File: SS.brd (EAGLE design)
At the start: 100 x 100 mm, 84 parts, among them K1 4052, K2 4052, Q1 SN74AHC-OR, Q2 UMD5N, Q3 UMD5N, Q4 SN74AHC-OR, Q5 BFP460, Q7 NCP553, Q8 TBD, X1 SO-239, X2 SO-239

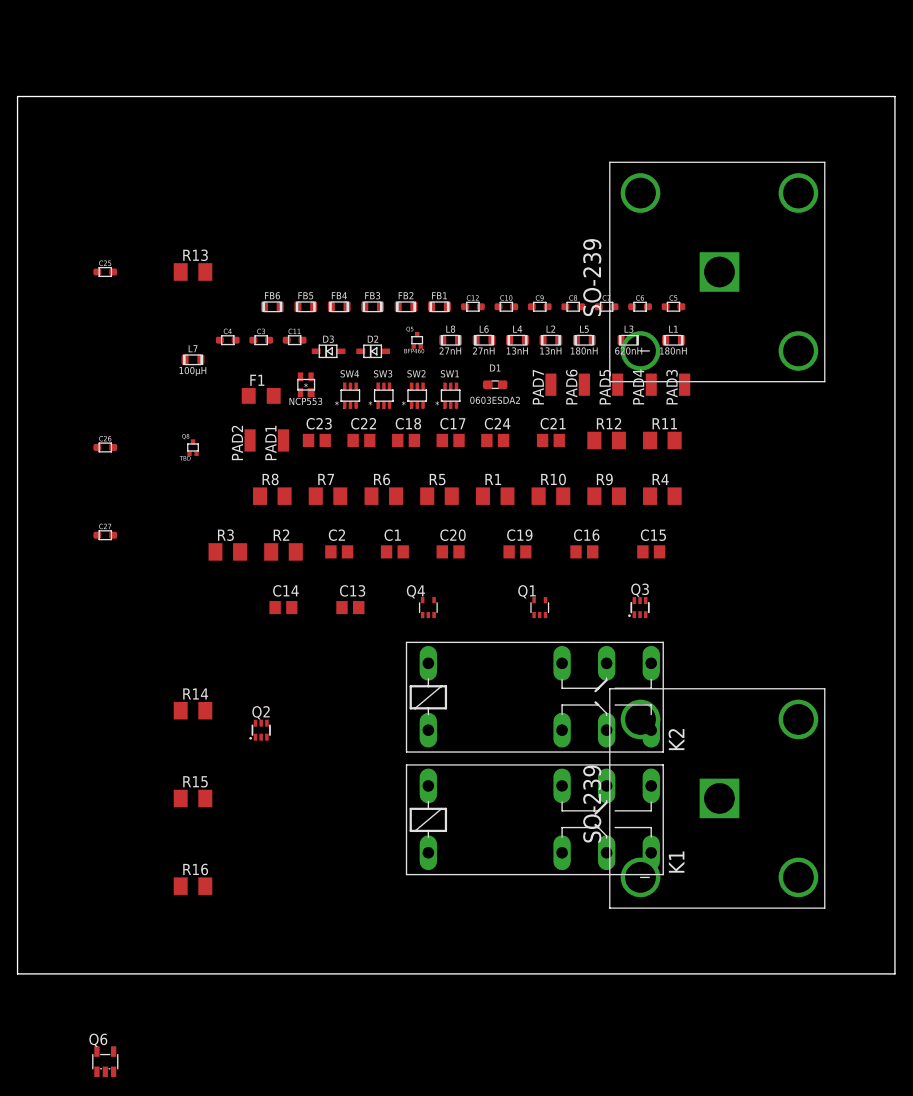
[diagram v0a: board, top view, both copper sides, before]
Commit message: Small minor improvements
* Corrected position of surge arrestor
* Added description for some networks
* Small improvements in component placement
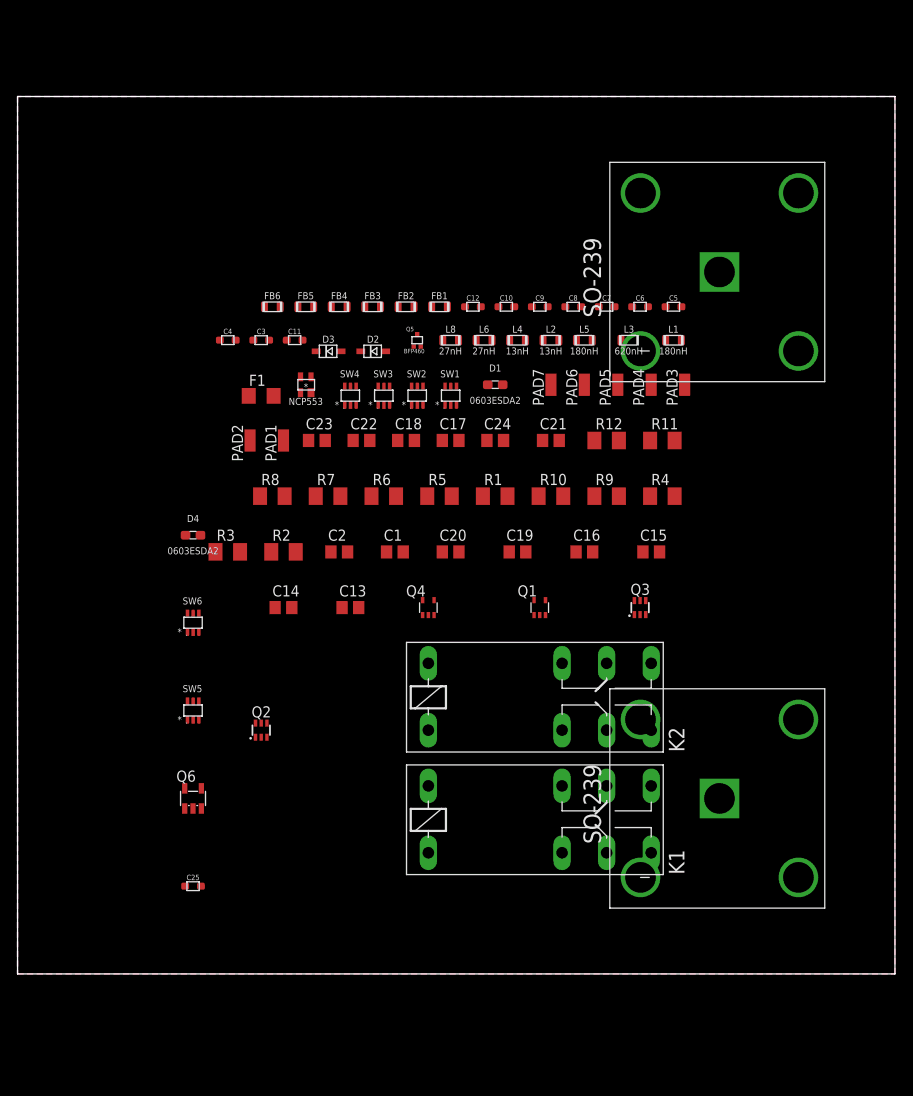
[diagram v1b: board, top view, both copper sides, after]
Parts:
- removed C26: 100pF, aarf:GRM18
- removed C27: 0.047µF, aarf:GRM18
- removed L7: 100µH, aarf:0805
- removed Q8: TBD, aarf:TSFP-3
- removed R13, R14: 4.7kΩ, rcl:M1206
- removed R15: 100Ω, rcl:M1206
- removed R16: 2.2kΩ, rcl:M1206
- added D4: 0603ESDA2, aarf:0603
- added SW5, SW6: (no value), aarf:SC-70
- C25: value 0.01µF -> 390pF
- moved C25 70.7 mm to (20.0, 10.0)
- moved Q6 31.6 mm to (20.0, 20.0)
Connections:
- net N$10 renamed LNA_IN
- net N$12 renamed FULL_BYP
- net N$15 renamed TX_INH
- net N$38 renamed BPF_OUT
- net N$43 renamed LNA_OUT
- net N$6 renamed LNA_BYPASS
- net UHF_ON renamed BPF_UHF
- removed net GPIO_OVERRIDE: FB6.P$2, Q4.2
- removed net N$29: C26.P$1, Q8.3, R16.2
- removed net N$30: C25.P$2, Q8.1, R13.2, R14.2
- removed net N$33: C27.P$2, R15.2, R16.1
- removed net N$37: C26.P$2, K1.S1, SW1.5
- removed net N$40: K2.S1, SW4.5
- new net BPF_IN: SW1.5, SW5.3
- new net FROM_BPF: D4.2, K2.S1, SW6.5
- new net LNA_OFF: Q4.4, SW3.4, SW4.4
- new net N$6: C25.P$2, SW5.5
- new net TO_BPF: C25.P$1, D1.2, K1.S1
- net 0: now also D4.1, SW5.1, SW5.2, SW6.1, SW6.2; no longer C25.P$1, C27.P$1, Q8.2, R14.1
- net 13.8V: no longer L7.P$2
- net 3V: now also SW5.6, SW6.6
- net AMP_OFF: now also FB6.P$2, Q4.2; no longer Q4.4, SW3.4, SW4.4
- net N$23: now also SW4.5, SW6.3; no longer L7.P$1, R15.1
- net N$8: no longer D1.2
- net RLY_BYPASS: now also SW5.4, SW6.4; no longer R13.1
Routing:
- added copper zone on layer 1, net GND
- added copper zone on layer 16, net GND

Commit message: More updates - refinements
* Added RF relays
* Simplified to a single relay driver (more than enough oomph to drive them both)
* New PNP-based driver for TX_GND
* Copious amount of signal direction and comments
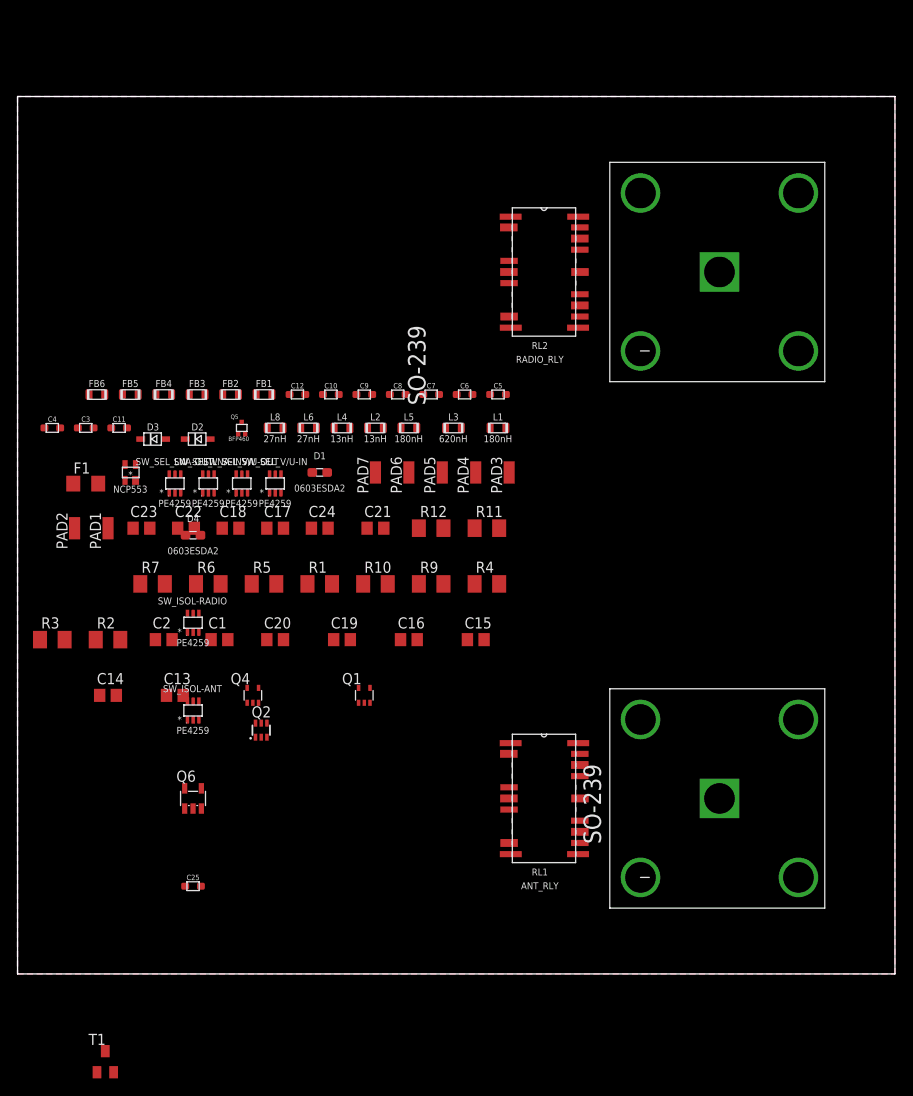
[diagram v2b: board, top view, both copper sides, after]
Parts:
- removed K1, K2: 4052, relay:F4052
- removed Q3: UMD5N, aarf:SOT363
- removed R8: 10kΩ, rcl:M1206
- removed SW1, SW2, SW3, SW4: (no value), aarf:SC-70
- added RL1: ANT_RLY, aarf:RELAY-TE-HF3
- added RL2: RADIO_RLY, aarf:RELAY-TE-HF3
- added SW_SEL_LNA-IN, SW_SEL_LNA-OUT, SW_SEL_V/U-IN, SW_SEL_V/U-OUT: PE4259, aarf:SC-70
- added T1: MMBTRA104SS, transistor:SC59-BEC
- PAD3: value RX -> TX_GND
- Q6: value (none) -> L78L05
- SW_ISOL-ANT, SW_ISOL-RADIO: value (none) -> PE4259
- moved L1 22.4 mm to (54.8, 62.2)
- moved L3 22.4 mm to (49.7, 62.2)
- moved C11 22.4 mm to (11.6, 62.2)
- moved C22 22.4 mm to (19.2, 50.8)
- moved C3 22.4 mm to (7.77, 62.2)
- moved C4 22.4 mm to (3.96, 62.2)
- moved C5 22.4 mm to (54.8, 66.0)
- moved D1 22.4 mm to (34.4, 57.1)
- moved FB1 22.4 mm to (28.1, 66.0)
- moved L2 22.4 mm to (40.8, 62.2)
- moved L4 22.4 mm to (37.0, 62.2)
- moved L6 22.4 mm to (33.2, 62.2)
- moved L8 22.4 mm to (29.4, 62.2)
- moved PAD3 22.4 mm to (56.0, 57.1)
- moved PAD4 22.4 mm to (52.2, 57.1)
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- renumbered SW5 to SW_ISOL-ANT, SW6 to SW_ISOL-RADIO
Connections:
- removed net 1: C18.1, D3.A, K2.2, R10.2
- removed net BPF_UHF: FB5.P$2, SW1.4, SW2.4
- removed net FROM_BPF: D4.2, K2.S1, SW_ISOL-RADIO.5
- removed net FULL_BYP: K1.O1, K2.O1
- removed net N$11: Q2.4, R9.1
- removed net N$2: K2.P1, X2.P$1
- removed net N$23: SW4.5, SW_ISOL-RADIO.3
- removed net N$34: C17.2, D2.C, K1.2, R9.2
- removed net N$35: Q3.2, Q3.3
- removed net N$39: Q3.4, R10.1
- removed net N$8: K1.P1, X1.P$1
- removed net TX_INH: FB2.P$2, K1.P2, K2.O2
- removed net TX_OFF: FB3.P$2, Q1.1
- new net AMP+BPF_OUT: D4.2, RL2.14, SW_ISOL-RADIO.5
- new net ANTENNA: RL1.6, X1.P$1
- new net DRIVE_TX: FB3.P$2, T1.B
- new net LNA-SW_OUT: SW_ISOL-RADIO.3, SW_SEL_LNA-OUT.5
- new net N$30: R10.2, RL2.1
- new net RADIO: RL2.6, X2.P$1
- new net RADIO_TX: Q1.1, T1.C
- new net RELAY-TO-RELAY_BYPASS: RL1.20, RL2.20
- new net RELAY_PWR: C17.2, C18.1, D2.C, D3.C, FB2.P$2, Q2.4, R10.1, R9.1
- new net SEL_BPF_UHF: FB5.P$2, SW_SEL_V/U-IN.4, SW_SEL_V/U-OUT.4
- net 0: now also D3.A, RL1.10, RL1.11, RL1.12, RL1.13, RL1.15, RL1.17, RL1.19, RL1.2, RL1.21, RL1.22, RL1.5, RL1.7, RL2.10, RL2.11, RL2.12, RL2.13, RL2.15, RL2.17, RL2.19, RL2.2, RL2.21, RL2.22, RL2.5, RL2.7, SW_SEL_LNA-IN.2, SW_SEL_LNA-OUT.2, SW_SEL_V/U-IN.2, SW_SEL_V/U-OUT.2; no longer D3.C, K1.1, K1.O2, K2.1, K2.P2, Q3.6, SW1.2, SW2.2, SW3.2, SW4.2
- net 13.8V: no longer Q3.1, R8.1
- net 3V: now also SW_SEL_LNA-IN.6, SW_SEL_LNA-OUT.6, SW_SEL_V/U-IN.6, SW_SEL_V/U-OUT.6, T1.E; no longer SW1.6, SW2.6, SW3.6, SW4.6
- net BPF_IN: now also SW_SEL_V/U-IN.5; no longer SW1.5
- net BPF_OUT: now also SW_SEL_LNA-IN.5, SW_SEL_V/U-OUT.5; no longer SW2.5, SW3.5
- net LNA_BYPASS: now also SW_SEL_LNA-IN.3, SW_SEL_LNA-OUT.3; no longer SW3.3, SW4.3
- net LNA_IN: now also SW_SEL_LNA-IN.1; no longer SW3.1
- net LNA_OFF: now also SW_SEL_LNA-IN.4, SW_SEL_LNA-OUT.4; no longer SW3.4, SW4.4
- net LNA_OUT: now also SW_SEL_LNA-OUT.1; no longer SW4.1
- net N$1: now also R9.2, RL1.1; no longer K1.S2, R8.2
- net N$21: now also SW_SEL_V/U-OUT.3; no longer SW2.3
- net N$3: now also SW_SEL_V/U-IN.1; no longer SW1.1
- net N$4: now also SW_SEL_V/U-IN.3; no longer SW1.3
- net N$7: now also SW_SEL_V/U-OUT.1; no longer SW2.1
- net RLY_BYPASS: no longer Q3.5
- net TO_BPF: now also RL1.14; no longer K1.S1

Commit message: Progress.
Schematic:
* Added pulldown resistors to input ports at OR comparator
* Added static bleeding on antenna-side isolation
* Replaced some 1206 caps with 0805

Board:
* Started arranging the first components.
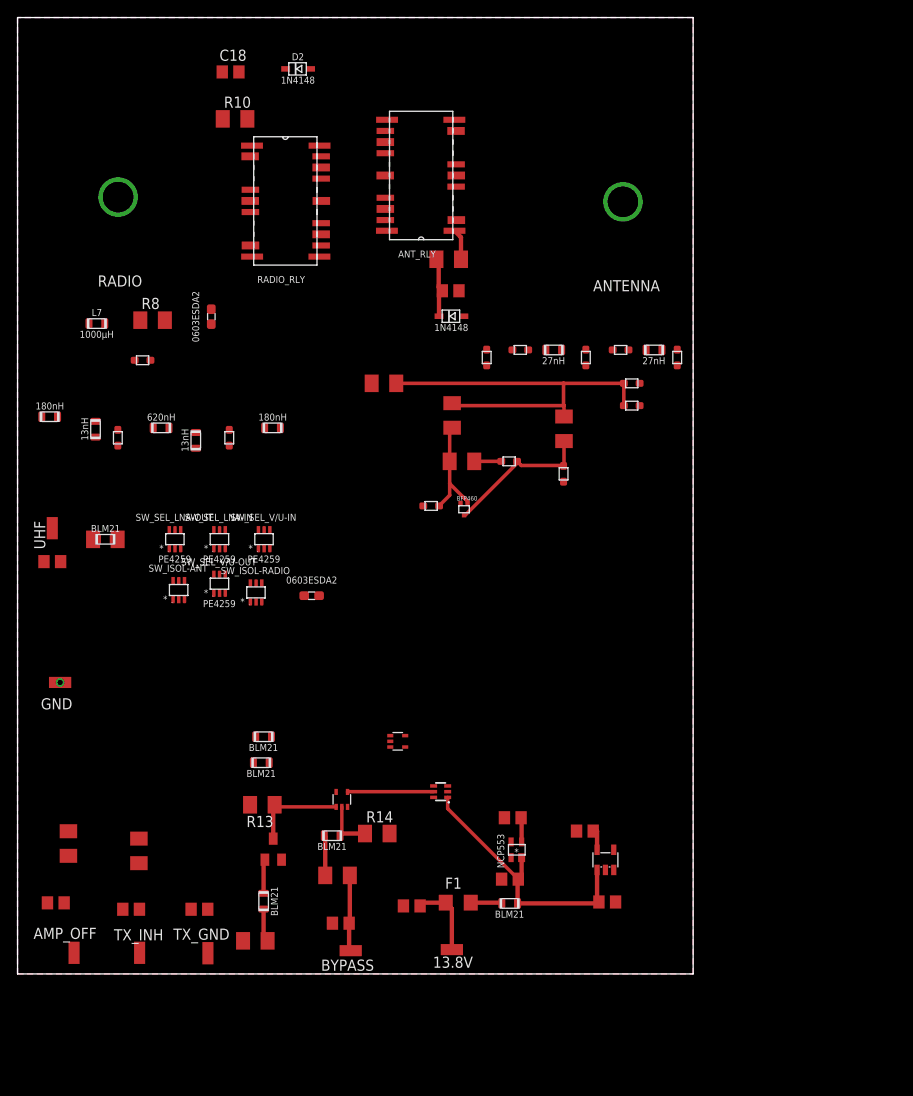
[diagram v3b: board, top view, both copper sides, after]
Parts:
- removed PAD1: 13.8V, wirepad:SMD1,27-2,54
- removed PAD2: TX INH, wirepad:SMD1,27-2,54
- removed PAD3: TX_GND, wirepad:SMD1,27-2,54
- removed PAD4: GND, wirepad:SMD1,27-2,54
- removed PAD5: BYPASS, wirepad:SMD1,27-2,54
- removed PAD6: UHF, wirepad:SMD1,27-2,54
- removed PAD7: AMP_OFF, wirepad:SMD1,27-2,54
- removed X1, X2: SO-239, aarf:SO-239
- added 13.8V: 13.8V, wirepad:SMD1,27-2,54
- added AMP_OFF: AMP_OFF, wirepad:SMD1,27-2,54
- added ANTENNA: ANTENNA, wirepad:SMD1,27-2,54
- added BYPASS: BYPASS, wirepad:SMD1,27-2,54
- added GND: GND, wirepad:SMD1,27-2,54
- added L7: 1000µH, aarf:0805
- added R13, R14: 10kΩ, rcl:M1206
- added R8: 1kΩ, rcl:M1206
- added RADIO: RADIO, wirepad:SMD1,27-2,54
- added TX_GND: TX_GND, wirepad:SMD1,27-2,54
- added TX_INH: TX INH, wirepad:SMD1,27-2,54
- added UHF: UHF, wirepad:SMD1,27-2,54
- C1, C2: device rcl:C0805 -> aarf:GRM18
- D2, D3: value (none) -> 1N4148
- F1: value (none) -> 1231
- FB1, FB2, FB3, FB4, FB5, FB6: value (none) -> BLM21
- moved RL1 72.4 mm to (46.0, 91.0), turned to 180 degrees
- moved FB1 64.4 mm to (56.1, 8.04)
- moved F1 63.9 mm to (50.2, 8.12), turned to 180 degrees
- moved R3 63.1 mm to (62.3, 62.1), turned to 90 degrees
- moved Q7 61.5 mm to (56.9, 14.2)
- moved C25 60.2 mm to (14.2, 69.9), turned to 180 degrees
- moved C11 58.6 mm to (70.0, 67.3)
- moved FB3 58.2 mm to (28.0, 8.29), turned to 90 degrees
- moved C23 58.0 mm to (56.1, 10.8)
- moved C22 57.1 mm to (64.7, 16.3)
- moved R10 55.4 mm to (24.8, 97.5)
- moved R12 54.8 mm to (5.80, 14.9), turned to 270 degrees
- moved C4 54.1 mm to (57.3, 71.1)
- moved FB4 53.8 mm to (35.9, 15.8)
- moved C18 52.0 mm to (24.3, 102.8)
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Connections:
- new net N$2: L7.P$1, R8.1
- net 0: no longer C1.1, C10.P$2, C11.P$2, C14.1, C15.1, C16.1, C17.1, C18.2, C19.1, C2.1, C20.1, C21.1, C22.1, C23.1, C24.1, C3.P$1, C6.P$1, C7.P$1, D1.1, D2.A, D3.A, D4.1, L2.P$2, L4.P$2, Q1.3, Q2.6, Q4.3, Q5.2, Q6.2, Q7.1, RL1.10, RL1.11, RL1.12, RL1.13, RL1.15, RL1.17, RL1.19, RL1.2, RL1.21, RL1.22, RL1.5, RL1.7, RL2.10, RL2.11, RL2.12, RL2.13, RL2.15, RL2.17, RL2.19, RL2.2, RL2.21, RL2.22, RL2.5, RL2.7, SW_ISOL-ANT.1, SW_ISOL-ANT.2, SW_ISOL-RADIO.1, SW_ISOL-RADIO.2, SW_SEL_LNA-IN.2, SW_SEL_LNA-OUT.2, SW_SEL_V/U-IN.2, SW_SEL_V/U-OUT.2, X1.P$2, X1.P$3, X1.P$4, X1.P$5, X2.P$2, X2.P$3, X2.P$4, X2.P$5
- net ANTENNA: now also ANTENNA.1; no longer X1.P$1
- net EXT_BYPASS: now also R14.1
- net GND: now also C1.P$1, C10.P$2, C11.P$2, C14.1, C15.1, C16.1, C17.1, C18.2, C19.1, C2.P$1, C20.1, C21.1, C22.1, C23.1, C24.1, C3.P$1, C6.P$1, C7.P$1, D1.1, D2.A, D3.A, D4.1, GND.1, L2.P$2, L4.P$2, L7.P$2, Q1.3, Q2.6, Q4.3, Q5.2, Q6.2, Q7.1, R13.2, R14.2, RL1.10, RL1.11, RL1.12, RL1.13, RL1.15, RL1.17, RL1.19, RL1.2, RL1.21, RL1.22, RL1.5, RL1.7, RL2.10, RL2.11, RL2.12, RL2.13, RL2.15, RL2.17, RL2.19, RL2.2, RL2.21, RL2.22, RL2.5, RL2.7, SW_ISOL-ANT.1, SW_ISOL-ANT.2, SW_ISOL-RADIO.1, SW_ISOL-RADIO.2, SW_SEL_LNA-IN.2, SW_SEL_LNA-OUT.2, SW_SEL_V/U-IN.2, SW_SEL_V/U-OUT.2; no longer PAD4.1
- net N$10: now also BYPASS.1; no longer PAD5.1
- net N$12: now also UHF.1; no longer PAD6.1
- net N$14: now also C2.P$2; no longer C2.2
- net N$15: now also AMP_OFF.1; no longer PAD7.1
- net N$16: now also TX_GND.1; no longer PAD3.1
- net N$26: now also TX_INH.1; no longer PAD2.1
- net N$5: now also C1.P$2; no longer C1.2
- net N$9: now also 13.8V.1; no longer PAD1.1
- net RADIO: now also RADIO.1; no longer X2.P$1
- net RADIO_TX: now also R13.1
- net TO_BPF: now also R8.2
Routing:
- net N$24: track 0.00 -> 45.2 mm
- net 13.8V: track 0.00 -> 31.4 mm
- net N$25: track 0.00 -> 17.0 mm
- net N$17: track 0.00 -> 12.6 mm
- net RADIO_TX: track 0.00 -> 11.0 mm
- net RLY_BYPASS: track 0.00 -> 9.82 mm
- net N$9: track 0.00 -> 8.72 mm
- net N$10: track 0.00 -> 8.69 mm
- net RELAY_PWR: track 0.00 -> 7.73 mm
- net EXT_BYPASS: track 0.00 -> 6.30 mm
- net N$32: track 0.00 -> 4.58 mm
- net DRIVE_TX: track 0.00 -> 3.89 mm
- net N$28: track 0.00 -> 3.81 mm
- net N$13: track 0.00 -> 3.57 mm
- net N$1: track 0.00 -> 3.56 mm
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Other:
- board size 100 x 100 mm -> 77 x 109 mm
